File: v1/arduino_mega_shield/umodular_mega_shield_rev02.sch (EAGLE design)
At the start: 29 parts, among them IC1 23LC1024, IC2 74HC4050/CD4050, IC3 6N138, U1 ARDUINO-MEGA-SHIELD

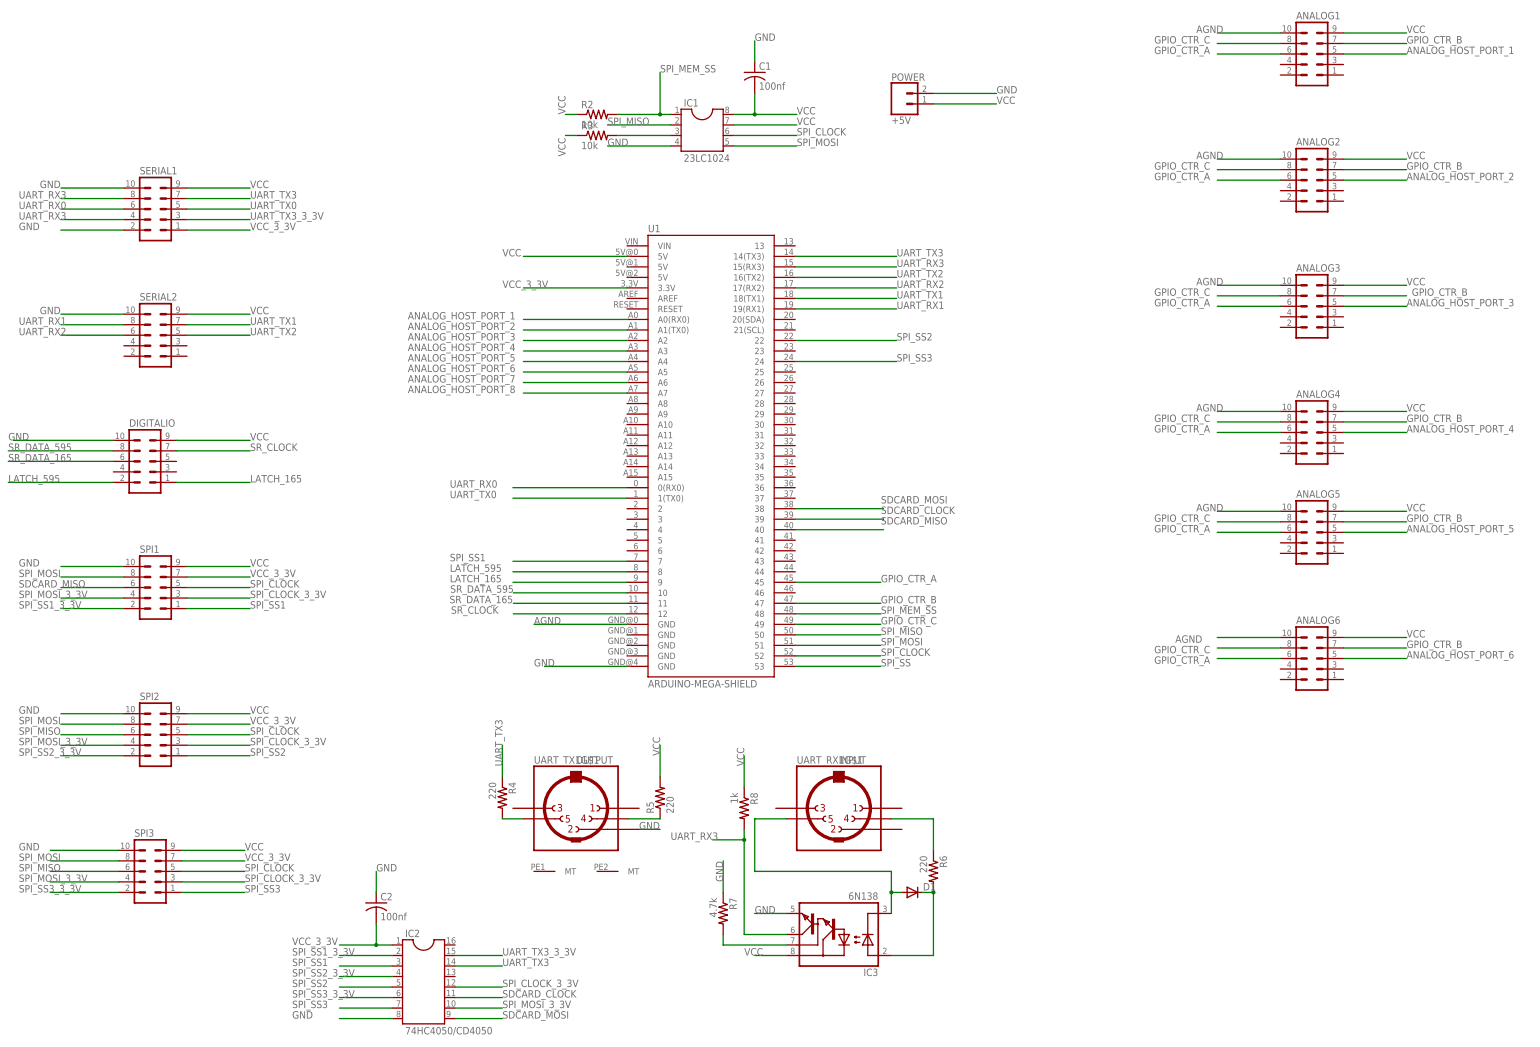
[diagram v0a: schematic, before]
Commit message: revert arduino mega shiled back to make use of SPI on shared subsystem
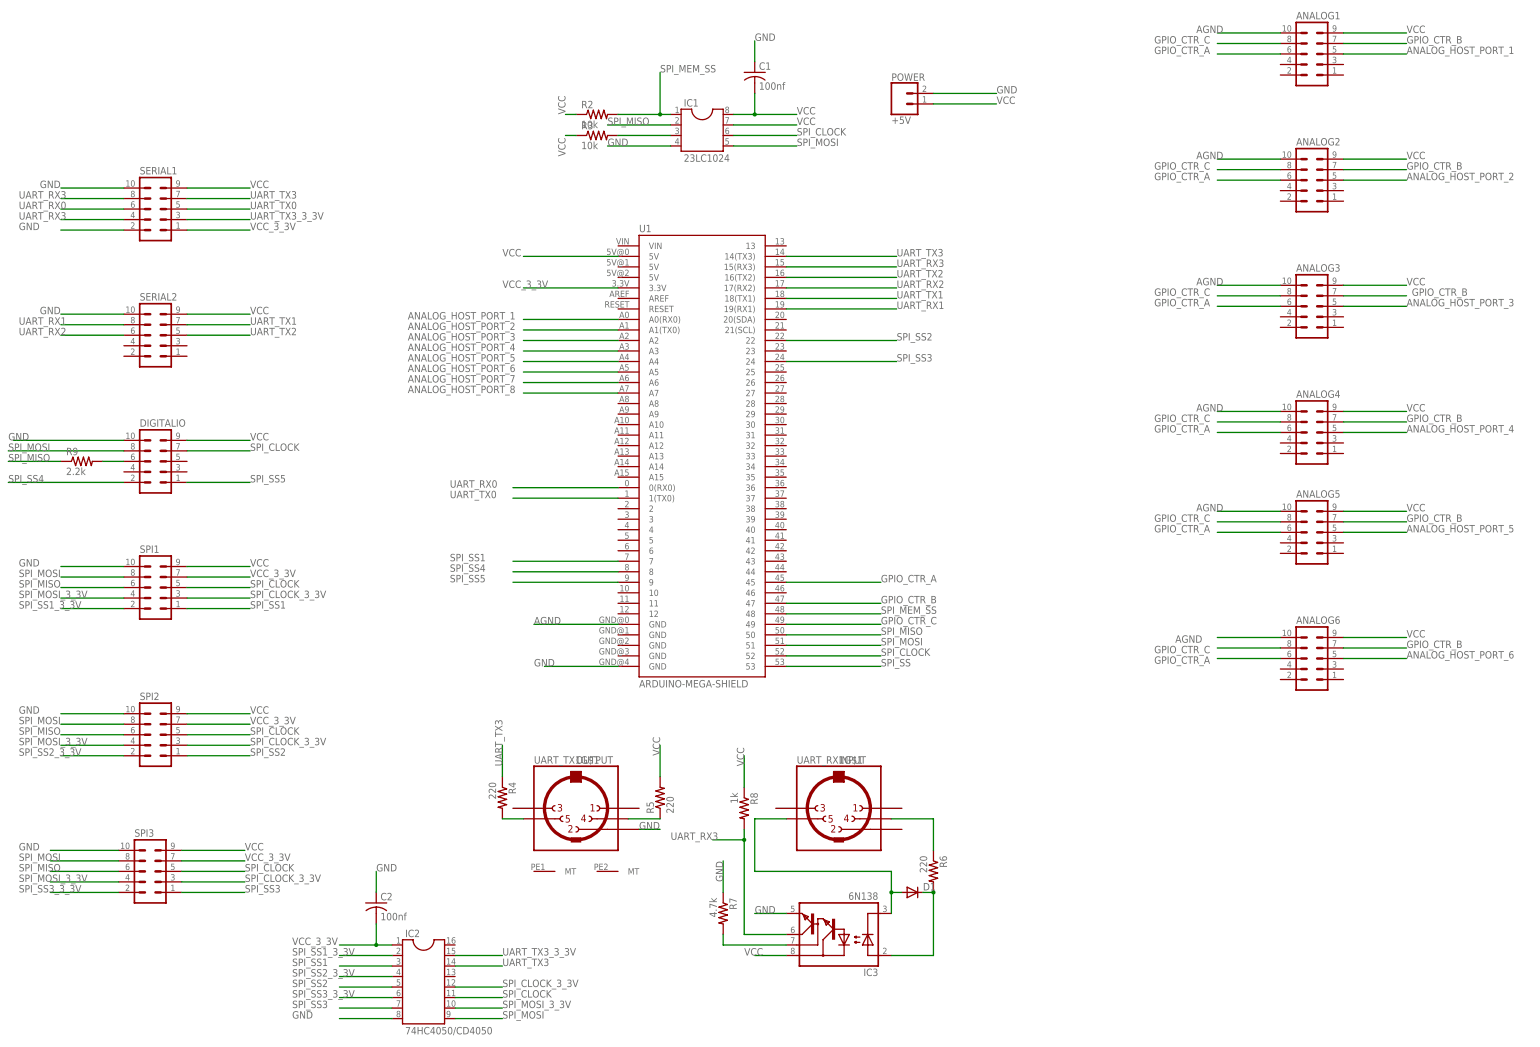
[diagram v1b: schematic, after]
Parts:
- added R9: 2.2k, rcl:R-US_0204/7
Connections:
- net LATCH_165 renamed SPI_SS5
- net LATCH_595 renamed SPI_SS4
- removed net SDCARD_CLOCK: IC2.11, U1.39
- removed net SDCARD_MISO: SPI1.6, U1.40
- removed net SDCARD_MOSI: IC2.9, U1.38
- removed net SR_CLOCK: DIGITALIO.7, U1.12
- removed net SR_DATA_165: DIGITALIO.6, U1.11
- removed net SR_DATA_595: DIGITALIO.8, U1.10
- new net N$9: DIGITALIO.6, R9.2
- net SPI_CLOCK: now also DIGITALIO.7, IC2.11
- net SPI_MISO: now also R9.1, SPI1.6
- net SPI_MOSI: now also DIGITALIO.8, IC2.9
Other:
- moved on the sheet: DIGITALIO, U1
